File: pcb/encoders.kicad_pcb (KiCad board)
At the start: 2 copper layers, 65 x 56.5 mm, 14 parts, among them J1 GPIO, J2 Screw_Terminal_01x04, J3 Screw_Terminal_01x04, J4 Screw_Terminal_01x04

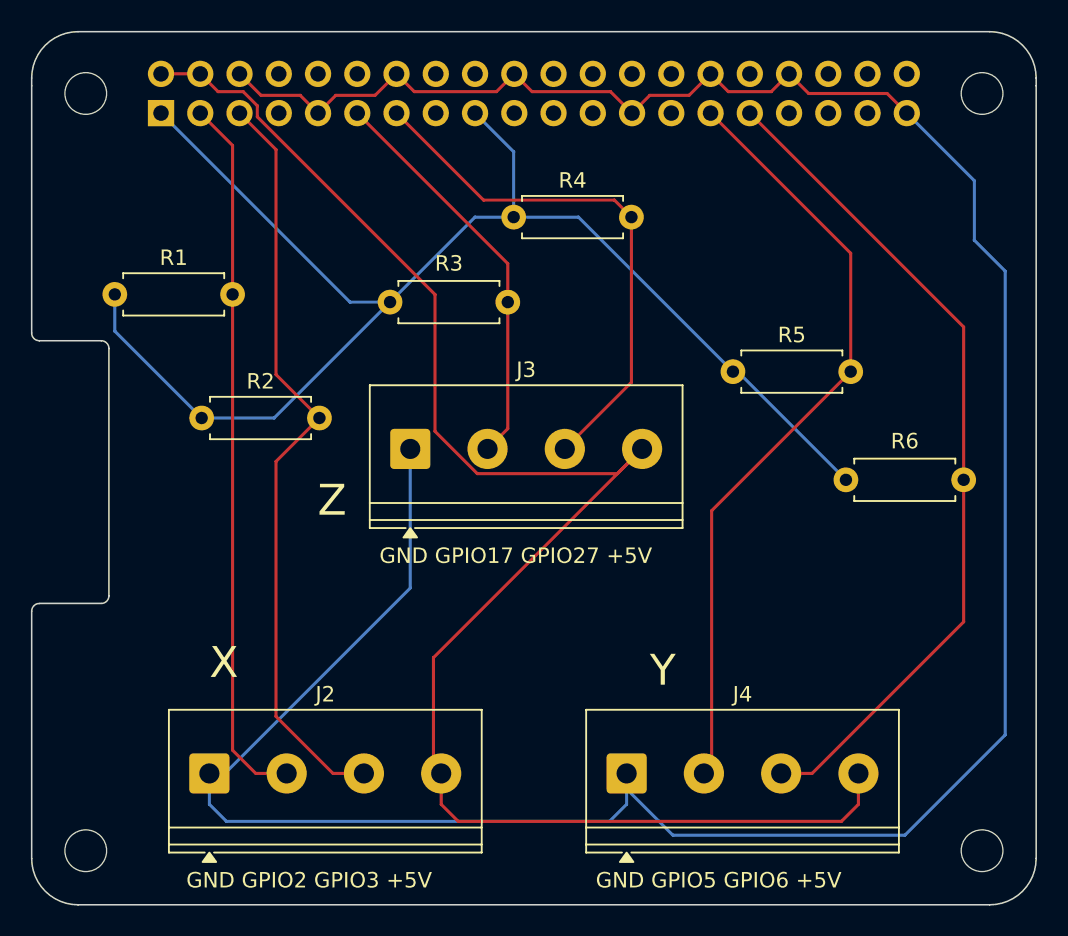
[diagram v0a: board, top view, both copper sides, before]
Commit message: update PCB to add two more terminals
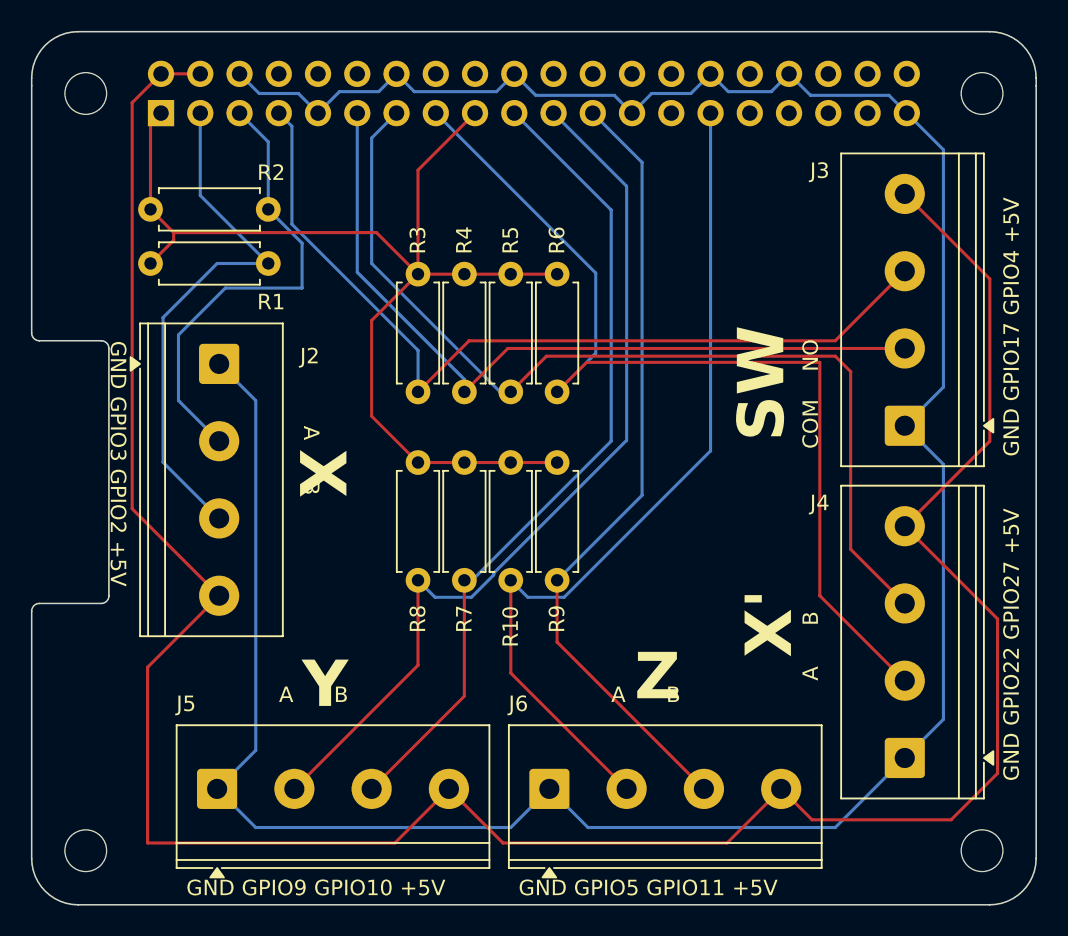
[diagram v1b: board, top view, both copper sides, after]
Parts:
- added J5: Screw_Terminal_01x04, TerminalBlock_Phoenix:TerminalBlock_Phoenix_PT-1,5-4-5.0-H_1x04_P5.00mm_Horizontal, F.Cu at (112.0, 92.5)
- added J6: Screw_Terminal_01x04, TerminalBlock_Phoenix:TerminalBlock_Phoenix_PT-1,5-4-5.0-H_1x04_P5.00mm_Horizontal, F.Cu at (133.5, 92.5)
- added R10: 4.7K, Resistor_THT:R_Axial_DIN0207_L6.3mm_D2.5mm_P7.62mm_Horizontal, F.Cu at (131.0, 71.4)
- added R7: 4.7K, Resistor_THT:R_Axial_DIN0207_L6.3mm_D2.5mm_P7.62mm_Horizontal, F.Cu at (128.0, 71.4)
- added R8: 4.7K, Resistor_THT:R_Axial_DIN0207_L6.3mm_D2.5mm_P7.62mm_Horizontal, F.Cu at (125.0, 71.4)
- added R9: 4.7K, Resistor_THT:R_Axial_DIN0207_L6.3mm_D2.5mm_P7.62mm_Horizontal, F.Cu at (134.0, 71.4)
- moved J3 32.0 mm to (156.5, 69.0), turned to 90 degrees
- moved J2 26.5 mm to (112.1, 65.0), turned to -90 degrees
- moved R6 22.9 mm to (134.0, 59.2), turned to -90 degrees
- moved J4 18.0 mm to (156.5, 90.5), turned to 90 degrees
- moved R5 15.7 mm to (131.0, 59.2), turned to -90 degrees
- moved R2 13.9 mm to (107.7, 55.0)
- moved R4 4.88 mm to (128.0, 59.2), turned to -90 degrees
- moved R1 3.06 mm to (107.7, 58.5)
- moved R3 2.56 mm to (125.0, 59.2), turned to -90 degrees
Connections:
- J2 pad 2: /GPIO2/SDA1 -> /GPIO3/SCL1
- J2 pad 3: /GPIO3/SCL1 -> /GPIO2/SDA1
- J3 pad 3: /GPIO27 -> /GPIO4/GPCLK0
- J4 pad 2: /GPIO5 -> /GPIO22
- J4 pad 3: /GPIO6 -> /GPIO27
- R3 pad 2: /GPIO17 -> /GPIO4/GPCLK0
- R4 pad 2: /GPIO27 -> /GPIO17
- R5 pad 2: /GPIO5 -> /GPIO27
- R6 pad 2: /GPIO6 -> /GPIO22
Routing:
- net /GPIO22: track 0.00 -> 64.0 mm
- net /GPIO9/SPI0.MISO: track 0.00 -> 58.2 mm
- net /GPIO4/GPCLK0: track 0.00 -> 56.5 mm
- net +5V: track 106.8 -> 163.3 mm
- net /GPIO6: track 54.5 -> 0.00 mm
- net /GPIO10/SPI0.MOSI: track 0.00 -> 53.0 mm
- net /GPIO11/SPI0.SCLK: track 0.00 -> 51.3 mm
- net /GPIO27: track 34.8 -> 62.7 mm
- net /GPIO17: track 26.3 -> 50.6 mm
- net +3V3: track 92.6 -> 72.8 mm
- net /GPIO3/SCL1: track 49.6 -> 30.2 mm
- net /GPIO2/SDA1: track 46.2 -> 34.3 mm
- net GND: track 181.5 -> 175.2 mm
- net /GPIO5: track 50.4 -> 55.8 mm
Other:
- board text added: "A B"
- board text added: "COM"
- board text added: "GND GPIO17 GPIO4 +5V"
- board text added: "GND GPIO22 GPIO27 +5V"
- board text added: "GND GPIO3 GPIO2 +5V"
- board text added: "GND GPIO5 GPIO11 +5V"
- board text added: "GND GPIO9 GPIO10 +5V"
- board text added: "NO"
- board text added: "SW"
- board text added: "X'"
- board text added: "https://github.com/scottfeldman/closinuf"
- board text removed: "GND GPIO17 GPIO27 +5V"
- board text removed: "GND GPIO2 GPIO3 +5V"
- board text removed: "GND GPIO5 GPIO6 +5V"

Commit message: updated schematic using ls7466s
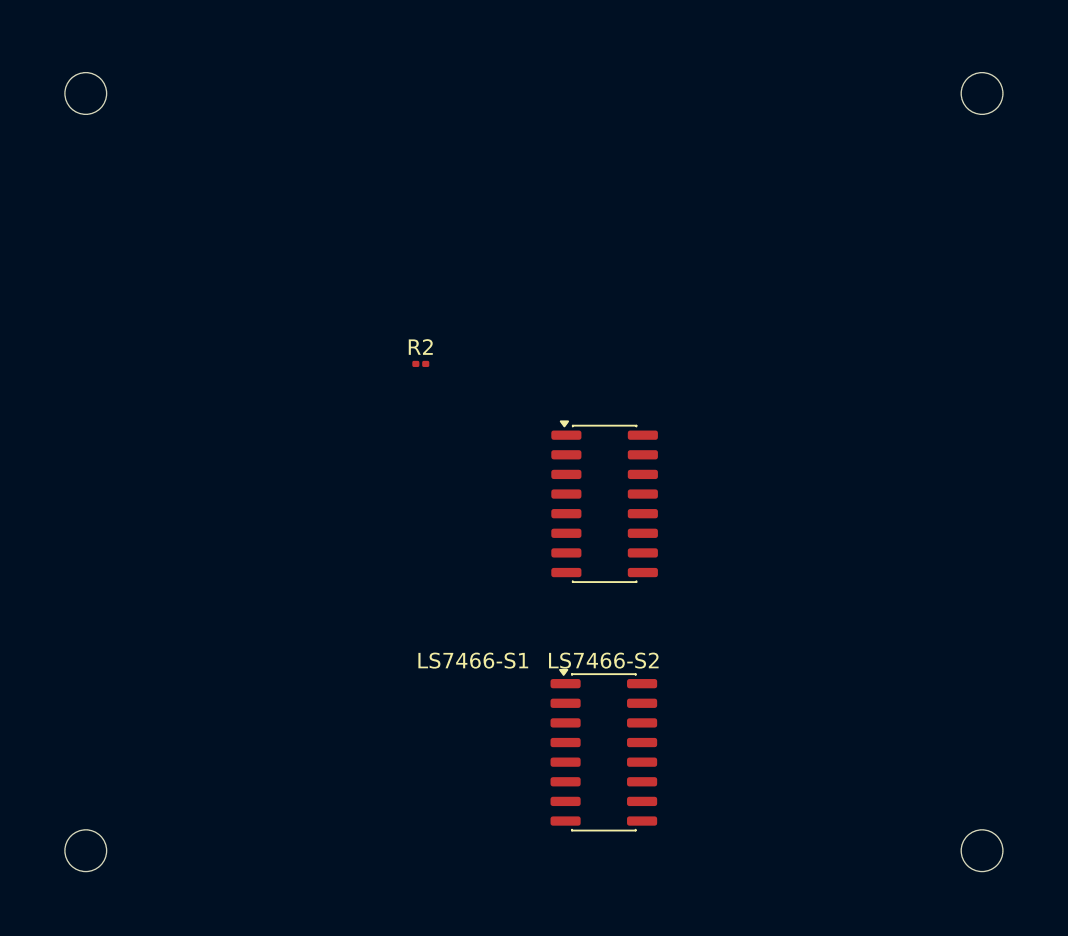
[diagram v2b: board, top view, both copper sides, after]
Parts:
- removed J1: GPIO, Connector_PinSocket_2.54mm:PinSocket_2x20_P2.54mm_Vertical
- removed J2, J3, J4, J5, J6: Screw_Terminal_01x04, TerminalBlock_Phoenix:TerminalBlock_Phoenix_PT-1,5-4-5.0-H_1x04_P5.00mm_Horizontal
- removed R1, R10, R3, R4, R5, R6, R7, R8, R9: 4.7K, Resistor_THT:R_Axial_DIN0207_L6.3mm_D2.5mm_P7.62mm_Horizontal
- added LS7466-S1: ~, Package_SO:SOIC-16_3.9x9.9mm_P1.27mm, F.Cu at (137.1, 74.1)
- added LS7466-S2: ~, Package_SO:SOIC-16_3.9x9.9mm_P1.27mm, F.Cu at (137.0, 90.1)
- R2: footprint Resistor_THT:R_Axial_DIN0207_L6.3mm_D2.5mm_P7.62mm_Horizontal -> Resistor_SMD:R_0201_0603Metric
- moved R2 20.1 mm to (125.2, 65.0)
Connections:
- R2 pad 1: +3V3 -> +3.3V
- R2 pad 2: /GPIO3/SCL1 -> Net-(J2-Pin_2)
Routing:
- net GND: track 175.2 -> 0.00 mm
- net +5V: track 163.3 -> 0.00 mm
- net +3V3: track 72.8 -> 0.00 mm
- net /GPIO22: track 64.0 -> 0.00 mm
- net /GPIO27: track 62.7 -> 0.00 mm
- net /GPIO9/SPI0.MISO: track 58.2 -> 0.00 mm
- net /GPIO4/GPCLK0: track 56.5 -> 0.00 mm
- net /GPIO5: track 55.8 -> 0.00 mm
- net /GPIO10/SPI0.MOSI: track 53.0 -> 0.00 mm
- net /GPIO11/SPI0.SCLK: track 51.3 -> 0.00 mm
- net /GPIO17: track 50.6 -> 0.00 mm
- net /GPIO2/SDA1: track 34.3 -> 0.00 mm
- net /GPIO3/SCL1: track 30.2 -> 0.00 mm
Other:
- board outline removed
- board text removed: "A B"
- board text removed: "COM"
- board text removed: "GND GPIO17 GPIO4 +5V"
- board text removed: "GND GPIO22 GPIO27 +5V"
- board text removed: "GND GPIO3 GPIO2 +5V"
- board text removed: "GND GPIO5 GPIO11 +5V"
- board text removed: "GND GPIO9 GPIO10 +5V"
- board text removed: "NO"
- board text removed: "RJ45"
- board text removed: "SW"
- board text removed: "USB"
- board text removed: "X"
- board text removed: "X'"
- board text removed: "Y"
- board text removed: "Z"
- board text removed: "https://github.com/scottfeldman/closinuf"
